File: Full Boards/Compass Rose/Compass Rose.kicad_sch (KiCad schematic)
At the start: 243 parts, among them J1 Program Header, Q10 2N3904, Q11 AO3401A, Q12 2N3904, Q7 AO3401A, Q8 2N3904, Q9 AO3401A, SW1 SW_MEC_5G, SW2 SW_MEC_5G, U1 ISO1044BD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

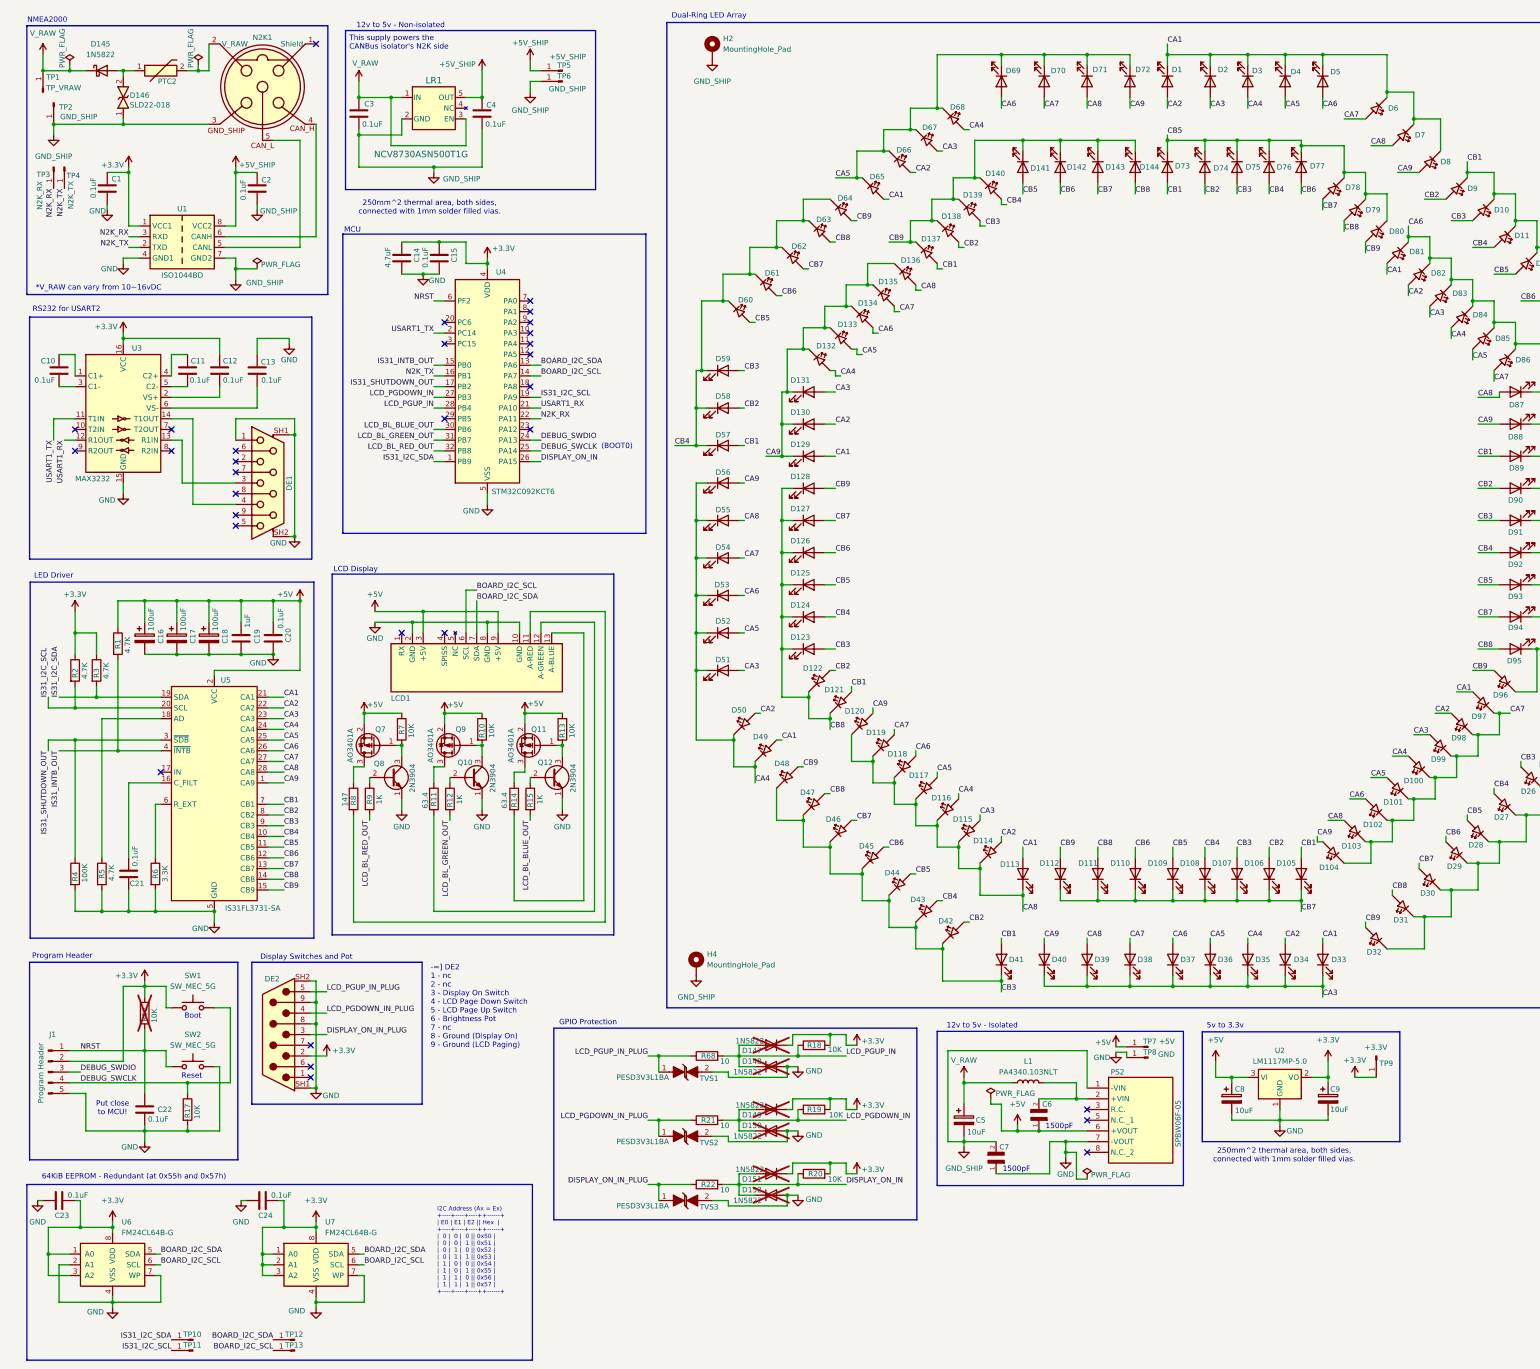
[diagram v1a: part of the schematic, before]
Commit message: Updated boards and schematics.
These are the version that have been ordered. Any further changes will be a new version.

Signed-off-by: Madison Kelly <digital.mermaid@gmail.com>
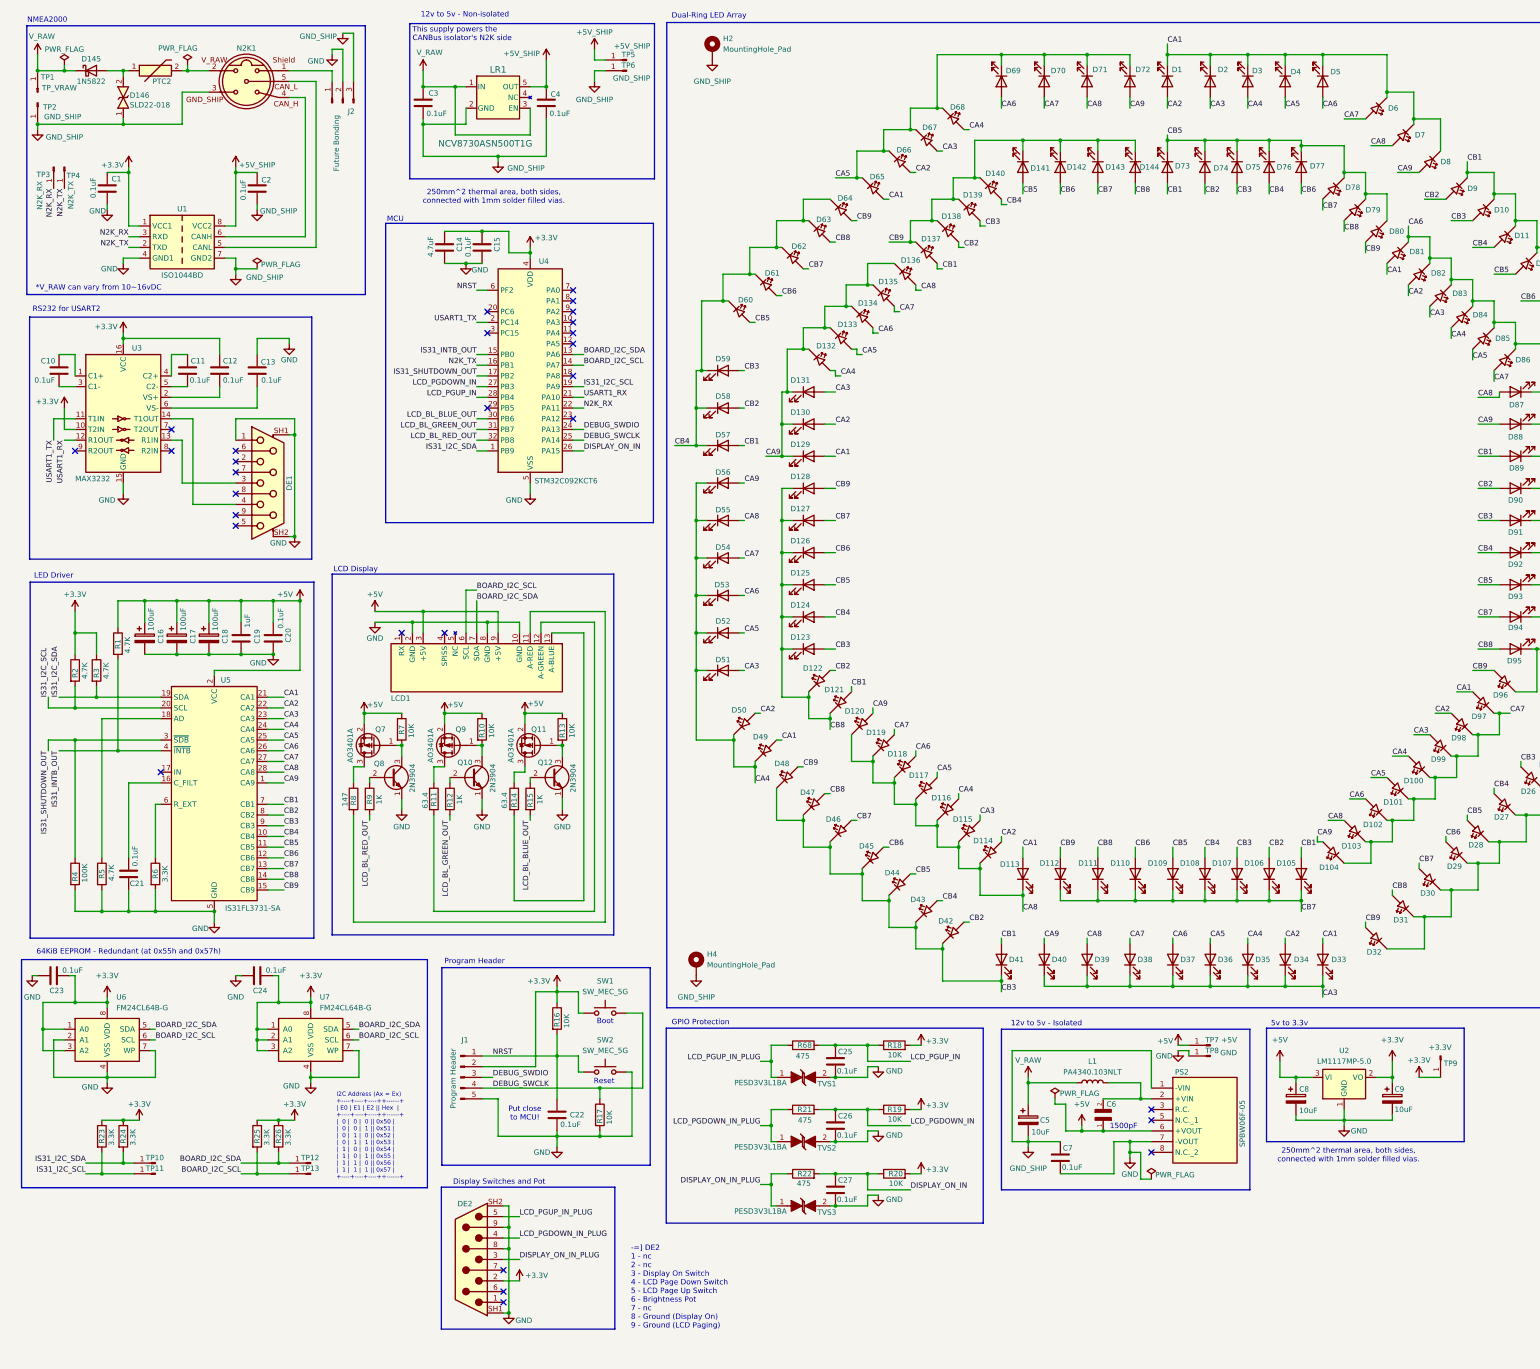
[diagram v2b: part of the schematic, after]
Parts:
- removed C7: TDK FA28NP01H152JNU06, FA28NP01H152JNU06:CAPRB500W50L400T250H550, symbol mr-parts:TDK FA28NP01H152JNU06
- removed D147, D148, D149, D150, D151, D152: 1N5822, Diode_THT:D_DO-41_SOD81_P10.16mm_Horizontal, symbol Diode:1N4001
- added C25, C26, C27, C7: 0.1uF, mr-stuff:RCE5C1H104J2A2H03B, symbol Device:C
- added J2: Future Bonding, Connector_PinHeader_2.54mm:PinHeader_1x03_P2.54mm_Vertical, symbol Connector:Conn_01x03_Pin
- added R23, R24, R25, R26: 3.3K, Resistor_THT:R_Axial_DIN0207_L6.3mm_D2.5mm_P7.62mm_Horizontal, symbol Device:R
- C6: footprint FA28NP01H152JNU06:CAPRB500W50L400T250H550 -> mr-stuff:TDK CAPRB500W50L400T250H550
- D146: footprint DIOAD4425W136L885D885 -> mr-stuff:DIOAD4425W136L885D885
- PS2: footprint SPBW06F05 -> mr-stuff:SPBW06F05
- R16: now fitted
- R21, R22, R68: value 10 -> 475
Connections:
- net +3.3V: now also U3.10 (T2IN), R23.1, R24.1, R25.1, R26.1
- net BOARD_I2C_SCL: now also R25.2
- net BOARD_I2C_SDA: now also R26.2
- net DISPLAY_ON_IN: now also C27.1
- net GND: now also C25.2, C26.2, C27.2, C7.2, J2.2 (Pin_2)
- net GND_SHIP: now also C7.1, J2.3 (Pin_3)
- net IS31_I2C_SCL: now also R23.2
- net IS31_I2C_SDA: now also R24.2
- net LCD_PGDOWN_IN: now also C26.1
- net LCD_PGUP_IN: now also C25.1
- net at N2K1.1: now also J2.1 (Pin_1)
- no-connect marks 31 -> 29
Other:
- note removed: "(BOOT0)"
- moved on the sheet: C14, C15, C22, C23, C24, C3, C4, C5, C6, C8, C9, D145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
